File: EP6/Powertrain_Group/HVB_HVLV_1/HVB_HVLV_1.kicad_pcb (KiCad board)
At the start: 2 copper layers, 132 x 62 mm, 20 parts, among them J1 HV+, J2 HV-, J3 from LV, J5 DCDC-, J6 DCDC+, K1 G7L-2A-X DC24, K2 DBT72410, Q1 IXTH6N100D2, U1 PC817

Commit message: update HVB_HVLV_1 V2.1
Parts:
- added D4: RED LED, LED_SMD:LED_0603_1608Metric, F.Cu at (109.9, 47.8)
- added D5: RED LED, LED_SMD:LED_0603_1608Metric, F.Cu at (109.9, 50.7)
- added D6: RED LED, LED_SMD:LED_0603_1608Metric, F.Cu at (109.9, 43.5)
- added D7: RED LED, LED_SMD:LED_0603_1608Metric, F.Cu at (109.9, 40.5)
- added J4: PrechargeRes-, nturt_kicad_lib_EP6:HRS_DF33C-2P-3.3DSA, F.Cu at (174.1, 75.0)
- added J7: PrechargeRes+, nturt_kicad_lib_EP6:HRS_DF33C-2P-3.3DSA, F.Cu at (174.1, 63.7)
- added R2: 10k, Resistor_SMD:R_0603_1608Metric, F.Cu at (112.1, 47.0)
- added R3: 10k, Resistor_SMD:R_0603_1608Metric, F.Cu at (111.4, 50.7)
- added R4: 10k, Resistor_SMD:R_0603_1608Metric, F.Cu at (111.4, 44.6)
- added R5: 10k, Resistor_SMD:R_0603_1608Metric, F.Cu at (110.7, 38.2)
- K1: value G7L-2A-X DC24 -> G2RG-2A-X DC24; footprint nturt_kicad_lib_EP6:RELAY_G7L-2A-X_OMR -> Relay_THT:Relay_DPST_Omron_G2RL-2A
- K2: value DBT72410 -> G2RG-2A-X DC24; footprint SamacSys_Parts_EP6:DBT72410 -> Relay_THT:Relay_DPST_Omron_G2RL-2A
- RV1: value 10k -> 10K; footprint PCM_Potentiometer_THT_AKL:Potentiometer_Bourns_3266W_Vertical -> nturt_kicad_lib_EP6:Throughhole Potentiometer 3296W
- moved R1 51.5 mm to (112.9, 50.7), turned to -90 degrees
- moved D3 51.4 mm to (127.3, 71.9), turned to 90 degrees
- moved D2 41.8 mm to (127.2, 30.9)
- moved J3 41.3 mm to (105.8, 40.5)
- moved H3 37.6 mm to (104.0, 91.0)
- moved H2 37.5 mm to (104.0, 29.0)
- moved J5 36.9 mm to (194.7, 37.5)
- moved K2 29.7 mm to (133.7, 70.6)
- moved D1 21.6 mm to (183.2, 64.3), turned to -90 degrees
- moved J6 16.2 mm to (194.7, 49.0)
- moved F3 13.8 mm to (170.0, 48.5)
- moved Q1 13.2 mm to (173.8, 88.5)
- moved U1 11.3 mm to (152.6, 80.8)
- moved K1 8.52 mm to (133.7, 39.3), turned to 90 degrees
- moved J2 7.09 mm to (166.0, 30.5)
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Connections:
- RV1 pad 1: Net-(Q1-G) -> Net-(Q1-S)
- RV1 pad 3: Net-(Q1-S) -> Net-(Q1-G)
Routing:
- net GND: track 105.0 -> 4.92 mm, vias 0 -> 4
- net /DCDC_CONTROL: track 85.2 -> 45.4 mm
- net Net-(J5-Pin_1): track 17.9 -> 45.6 mm
- net Net-(J7-Pin_1): track 0.00 -> 26.8 mm
- net /HVpresent: track 86.9 -> 62.0 mm
- net /HV+: track 85.6 -> 110.0 mm
- net Net-(J4-Pin_1): track 0.00 -> 21.2 mm
- net +5V: track 79.9 -> 60.2 mm
- net /HV-: track 86.4 -> 68.7 mm
- net Net-(D1-K): track 6.97 -> 20.7 mm
- net /DC_CONTROL: track 48.0 -> 53.0 mm
- net Net-(Q1-S): track 20.3 -> 23.7 mm
- net Net-(F3-Pad2): track 12.5 -> 9.23 mm
- net Net-(D1-A): track 7.53 -> 10.6 mm
- net Net-(Q1-G): track 28.3 -> 25.9 mm
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- added copper zone on B.Cu, net GND
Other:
- board size 132 x 62 mm -> 100 x 70 mm
- board text added: "DCDC relay"
- board text added: "DISCHARGE"
- board text added: "Discharge relay"
- board text added: "EP6 HVB_HVLV_1 ver 2.1 25/03/11 Jack Kuo"
- board text added: "RTM FUSE (DCDC)"
- board text removed: "EP6 HVB_HVLV_1 ver 1.0 Jack Kuo"
- board text removed: "RTM FUSE"

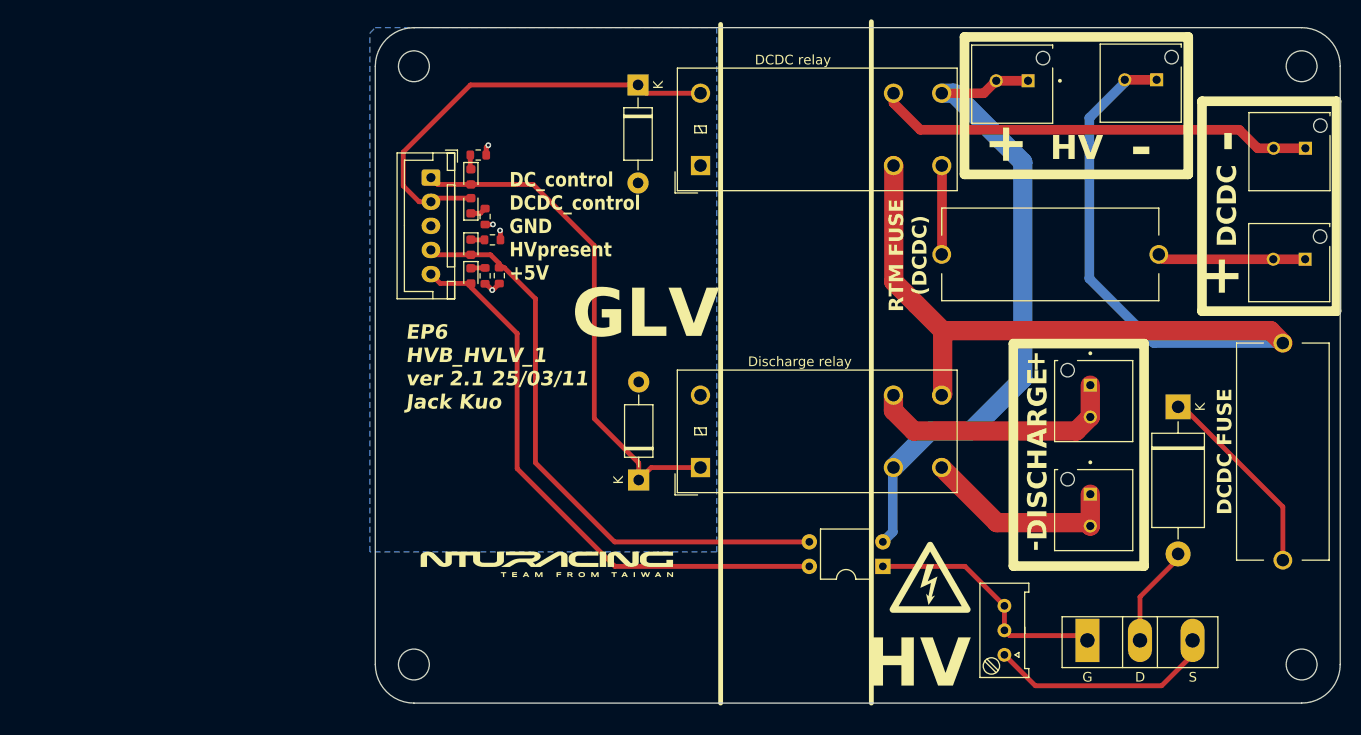
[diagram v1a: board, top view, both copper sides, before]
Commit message: update HVB_HVLV_1 to V2.2
V2.2 remove discharge relay
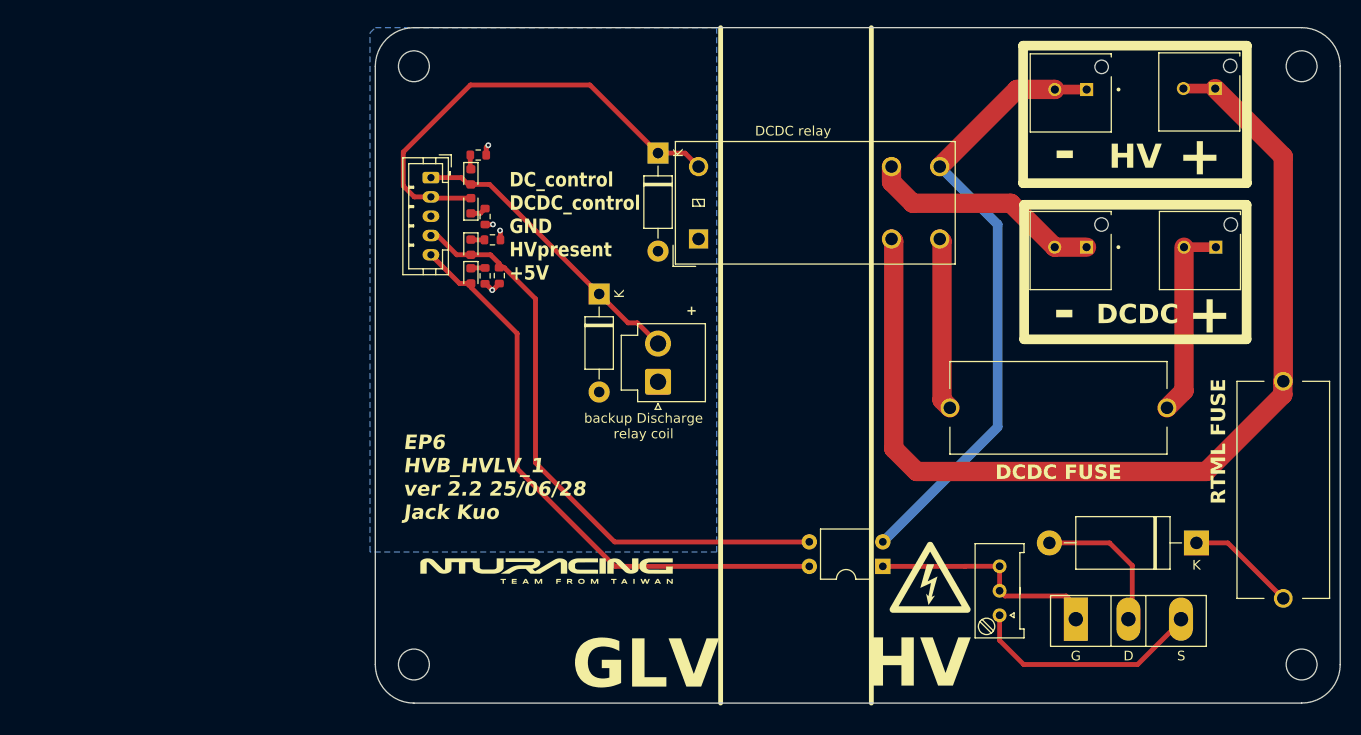
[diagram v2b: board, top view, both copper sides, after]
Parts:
- removed J7: PrechargeRes+, nturt_kicad_lib_EP6:HRS_DF33C-2P-3.3DSA
- removed K2: G2RG-2A-X DC24, Relay_THT:Relay_DPST_Omron_G2RL-2A
- J3: footprint Connector_JST:JST_XH_B5B-XH-A_1x05_P2.50mm_Vertical -> Connector_JST:JST_PH_B5B-PH-K_1x05_P2.00mm_Vertical
- J4: value PrechargeRes- -> DC_CONTROL_COIL; footprint nturt_kicad_lib_EP6:HRS_DF33C-2P-3.3DSA -> Connector_JST:JST_VH_B2P-VH_1x02_P3.96mm_Vertical
- moved J4 46.7 mm to (129.3, 61.7)
- moved J5 24.9 mm to (172.1, 47.8)
- moved D3 19.7 mm to (123.2, 52.6), turned to -90 degrees
- moved F3 15.9 mm to (170.8, 64.4)
- moved D1 14.2 mm to (185.1, 78.4), turned to 180 degrees
- moved J6 9.34 mm to (185.5, 47.8)
- moved K1 7.61 mm to (133.5, 46.9)
- moved D2 7.36 mm to (129.3, 38.0)
- moved J2 6.14 mm to (172.1, 31.4)
- moved J1 6.14 mm to (185.4, 31.3)
- moved RV1 4.13 mm to (164.7, 85.9)
- moved F1 3.96 mm to (194.1, 72.9)
- moved Q1 2.51 mm to (172.6, 86.3)
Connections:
- net Net-(J5-Pin_1) renamed /DCDC-
- net Net-(J6-Pin_1) renamed /DCDC+
- J4 pad 1: Net-(J4-Pin_1) -> GND
- J4 pad 2: Net-(J4-Pin_1) -> /DC_CONTROL
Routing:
- net Net-(J7-Pin_1): track 26.8 -> 0.00 mm
- net /DC_CONTROL: track 53.0 -> 30.7 mm
- net Net-(J4-Pin_1): track 21.2 -> 0.00 mm
- net /DCDC-: track 45.6 -> 24.6 mm
- net Net-(D1-K): track 20.7 -> 11.4 mm
- net Net-(F3-Pad2): track 9.23 -> 17.9 mm
- net /HV+: track 110.0 -> 104.4 mm
- net /DCDC+: track 15.4 -> 20.7 mm
- net Net-(D1-A): track 10.6 -> 15.3 mm
- net /HV-: track 68.7 -> 64.8 mm
- net /DCDC_CONTROL: track 45.4 -> 48.0 mm
- net Net-(Q1-G): track 25.9 -> 24.6 mm
- net Net-(Q1-S): track 23.7 -> 24.5 mm
- net +5V: track 60.2 -> 61.0 mm
- net /HVpresent: track 62.0 -> 62.6 mm
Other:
- board text added: "EP6 HVB_HVLV_1 ver 2.2 25/06/28 Jack Kuo"
- board text added: "RTML FUSE"
- board text added: "backup Discharge relay coil"
- board text removed: "DISCHARGE"
- board text removed: "Discharge relay"
- board text removed: "EP6 HVB_HVLV_1 ver 2.1 25/03/11 Jack Kuo"
- board text removed: "RTM FUSE (DCDC)"
